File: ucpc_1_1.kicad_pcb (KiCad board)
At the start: 4 copper layers, 55.9 x 62.8 mm, 93 parts, among them J1 Micro_SD_Card_Det, J10 pck, J11 hs, J12 vs, J13 xck, J2 Audio-Jack-4, J3 DISPLAY, J4 POWER, J5 DEBUG, J6 RJ45_LEDS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

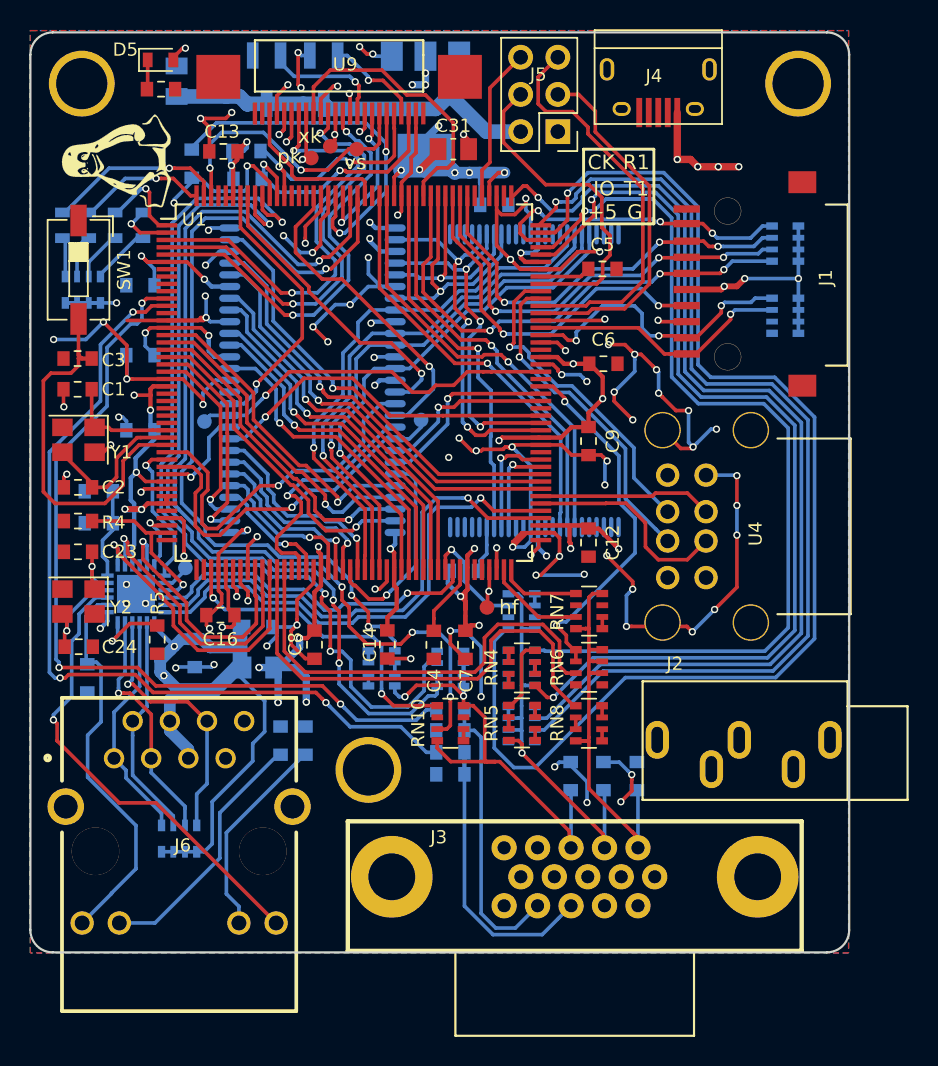
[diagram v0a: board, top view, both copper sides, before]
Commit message: convert to KiCad 6 format
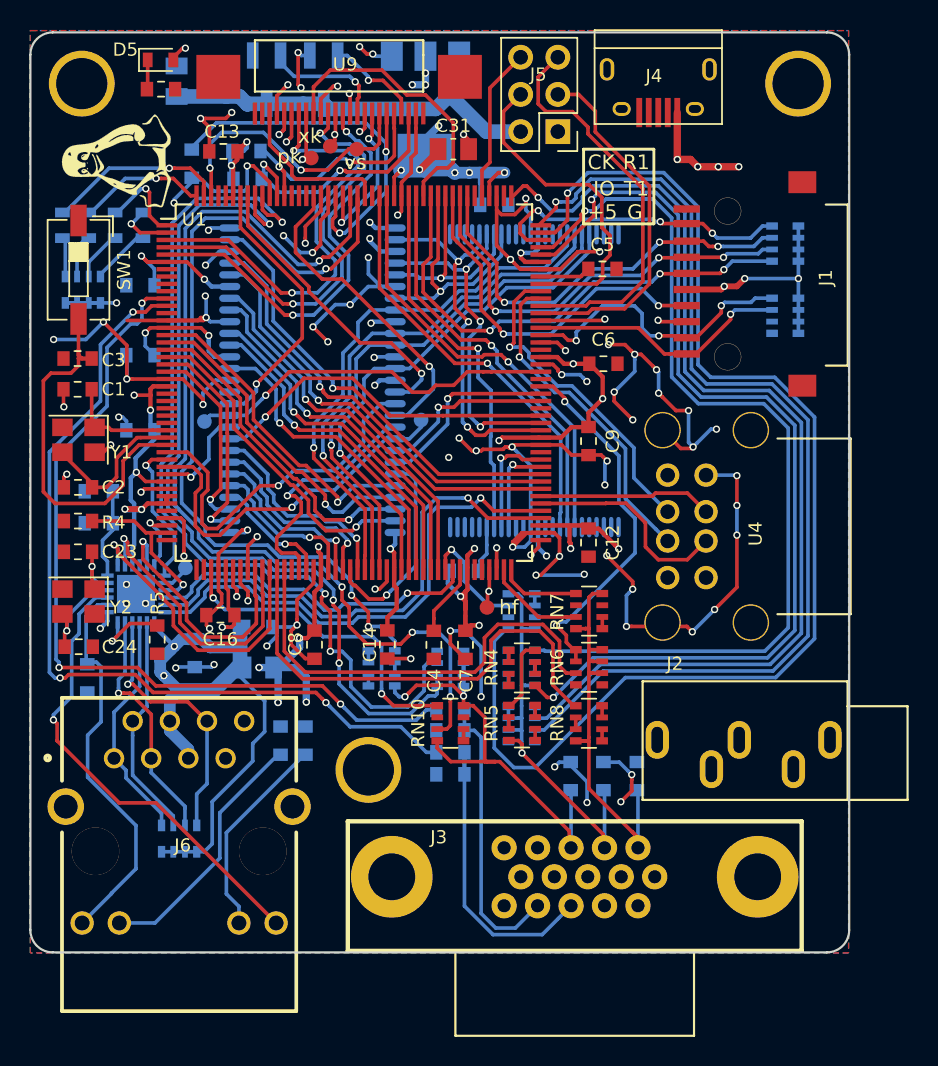
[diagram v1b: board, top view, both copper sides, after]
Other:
- net class Default removed
